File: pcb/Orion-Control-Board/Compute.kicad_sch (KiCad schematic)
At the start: 20 parts, among them J10 POWER, J2 NUCLEO64_CN7, J3 JETSON_ORIN_NANO_DEVKIT_GPIO, J4 5V Select Socket, J5 5V Select Jumper, J6 NUCLEO64_CN10, J7 I2C 1, J8 I2C 3, J9 UART

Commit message: Update symbols
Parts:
- J10, J5, J7, J8, J9: footprint AA_Custom_Components:Jumper_PinHeader_1x03_P2.54mm_Vertical -> digikey-footprints:PinHeader_1x3_P2.54_Drill1.1mm
- J4: footprint Connector_PinSocket_2.54mm:PinSocket_1x03_P2.54mm_Vertical -> digikey-footprints:PinHeader_1x3_P2.54_Drill1.1mm
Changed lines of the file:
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@@
 	)
 	(symbol
-		(lib_name "MountingHole_4")
 		(lib_id "Mechanical:MountingHole")
 		(at 162.56 25.4 0)
@@
 			)
 		)
-		(property "Description" ""
+		(property "Description" "Mounting Hole without connection"
 			(at 162.56 25.4 0)
 			(effects
@@
 					(size 1.27 1.27)
 				)
+				(hide yes)
 			)
 		)
@@
 	)
 	(symbol
-		(lib_name "MountingHole_3")
 		(lib_id "Mechanical:MountingHole")
 		(at 182.88 25.4 0)
@@
 			)
 		)
-		(property "Description" ""
+		(property "Description" "Mounting Hole without connection"
 			(at 182.88 25.4 0)
 			(effects
@@
 					(size 1.27 1.27)
 				)
+				(hide yes)
 			)
 		)
@@
 	)
 	(symbol
-		(lib_name "MountingHole_2")
 		(lib_id "Mechanical:MountingHole")
 		(at 162.56 31.75 0)
@@
 			)
 		)
-		(property "Description" ""
+		(property "Description" "Mounting Hole without connection"
 			(at 162.56 31.75 0)
 			(effects
@@
 					(size 1.27 1.27)
 				)
+				(hide yes)
 			)
 		)
@@
 	)
 	(symbol
-		(lib_name "MountingHole_1")
 		(lib_id "Mechanical:MountingHole")
 		(at 182.88 31.75 0)
@@
 			)
 		)
-		(property "Description" ""
+		(property "Description" "Mounting Hole without connection"
 			(at 182.88 31.75 0)
 			(effects
@@
 					(size 1.27 1.27)
 				)
+				(hide yes)
 			)
 		)
@@
 	)
 	(symbol
-		(lib_name "MountingHole_2")
 		(lib_id "Mechanical:MountingHole")
 		(at 229.87 25.4 0)
@@
 			)
 		)
-		(property "Description" ""
+		(property "Description" "Mounting Hole without connection"
 			(at 229.87 25.4 0)
 			(effects
@@
 			)
 		)
-		(property "Description" ""
+		(property "Description" "Power symbol creates a global label with name \"+5VD\""
 			(at 125.73 72.39 0)
 			(effects
@@
 					(size 1.27 1.27)
 				)
+				(hide yes)
 			)
 		)
@@
 			)
 		)
-		(property "Footprint" "AA_Custom_Components:Jumper_PinHeader_1x03_P2.54mm_Vertical"
+		(property "Footprint" "digikey-footprints:PinHeader_1x3_P2.54_Drill1.1mm"
 			(at 152.4 72.39 0)
 			(effects
@@
 			)
 		)
-		(property "Description" ""
+		(property "Description" "Ground Supply (Earth Ground style) Ground supply with a traditional \"earth ground\" symbol."
 			(at 172.72 72.39 0)
 			(effects
@@
 					(size 1.27 1.27)
 				)
+				(hide yes)
 			)
 		)
@@
 			)
 		)
-		(property "Description" ""
+		(property "Description" "Power symbol creates a global label with name \"+3.3V\""
 			(at 185.42 87.63 0)
 			(effects
@@
 					(size 1.27 1.27)
 				)
+				(hide yes)
 			)
 		)
@@
 	)
 	(symbol
-		(lib_name "MountingHole_3")
 		(lib_id "Mechanical:MountingHole")
 		(at 208.28 25.4 0)
@@
 			)
 		)
-		(property "Description" ""
+		(property "Description" "Mounting Hole without connection"
 			(at 208.28 25.4 0)
 			(effects
@@
 			)
 		)
-		(property "Description" ""
+		(property "Description" "Power symbol creates a global label with name \"+5VD\""
 			(at 64.77 68.58 0)
 			(effects
@@
 					(size 1.27 1.27)
 				)
+				(hide yes)
 			)
 		)
@@
 			)
 		)
-		(property "Description" ""
+		(property "Description" "Ground Supply (Earth Ground style) Ground supply with a traditional \"earth ground\" symbol."
 			(at 149.86 90.17 0)
 			(effects
@@
 					(size 1.27 1.27)
 				)
+				(hide yes)
 			)
 		)
@@
 			)
 		)
-		(property "Description" ""
+		(property "Description" "Ground Supply (Earth Ground style) Ground supply with a traditional \"earth ground\" symbol."
 			(at 149.86 72.39 0)
 			(effects
@@
 					(size 1.27 1.27)
 				)
+				(hide yes)
 			)
 		)
@@
 			)
 		)
-		(property "Description" ""
+		(property "Description" "Ground Supply (Earth Ground style) Ground supply with a traditional \"earth ground\" symbol."
 			(at 125.73 87.63 0)
 			(effects
@@
 					(size 1.27 1.27)
 				)
+				(hide yes)
 			)
 		)
@@
 			)
 		)
-		(property "Description" ""
+		(property "Description" "test point"
 			(at 128.27 22.86 0)
 			(effects
@@
 			)
 		)
-		(property "Description" ""
+		(property "Description" "Power symbol creates a global label with name \"+3.3V\""
 			(at 60.96 81.28 0)
 			(effects
@@
 					(size 1.27 1.27)
 				)
+				(hide yes)
 			)
 		)
@@
 			)
 		)
-		(property "Description" ""
+		(property "Description" "Power symbol creates a global label with name \"+5VD\""
 			(at 111.76 22.86 0)
 			(effects
@@
 					(size 1.27 1.27)
 				)
+				(hide yes)
 			)
 		)
@@
 			)
 		)
-		(property "Description" ""
+		(property "Description" "test point"
 			(at 111.76 22.86 0)
 			(effects
@@
 			)
 		)
-		(property "Description" ""
+		(property "Description" "test point"
 			(at 144.78 20.32 0)
 			(effects
@@
 			)
 		)
-		(property "Footprint" "Connector_PinSocket_2.54mm:PinSocket_1x03_P2.54mm_Vertical"
+		(property "Footprint" "digikey-footprints:PinHeader_1x3_P2.54_Drill1.1mm"
 			(at 102.87 34.29 0)
 			(effects
@@
 			)
 		)
-		(property "Description" ""
+		(property "Description" "Power symbol creates a global label with name \"+5VD\""
 			(at 179.07 85.09 0)
 			(effects
@@
 					(size 1.27 1.27)
 				)
+				(hide yes)
 			)
 		)
@@
 			)
 		)
-		(property "Footprint" "AA_Custom_Components:Jumper_PinHeader_1x03_P2.54mm_Vertical"
+		(property "Footprint" "digikey-footprints:PinHeader_1x3_P2.54_Drill1.1mm"
 			(at 175.26 90.17 0)
 			(effects
@@
 			)
 		)
-		(property "Description" ""
+		(property "Description" "Power symbol creates a global label with name \"+3.3V\""
 			(at 128.27 22.86 0)
 			(effects
@@
 					(size 1.27 1.27)
 				)
+				(hide yes)
 			)
 		)
@@
 			)
 		)
-		(property "Footprint" "AA_Custom_Components:Jumper_PinHeader_1x03_P2.54mm_Vertical"
+		(property "Footprint" "digikey-footprints:PinHeader_1x3_P2.54_Drill1.1mm"
 			(at 152.4 90.17 0)
 			(effects
@@
 			)
 		)
-		(property "Description" ""
+		(property "Description" "Ground Supply (Earth Ground style) Ground supply with a traditional \"earth ground\" symbol."
 			(at 17.78 86.36 0)
 			(effects
@@
 					(size 1.27 1.27)
 				)
+				(hide yes)
 			)
 		)
@@
 			)
 		)
-		(property "Description" ""
+		(property "Description" "Ground Supply (Earth Ground style) Ground supply with a traditional \"earth ground\" symbol."
 			(at 62.23 104.14 0)
 			(effects
@@
 					(size 1.27 1.27)
 				)
+				(hide yes)
 			)
 		)
@@
 			)
 		)
-		(property "Footprint" "AA_Custom_Components:Jumper_PinHeader_1x03_P2.54mm_Vertical"
+		(property "Footprint" "digikey-footprints:PinHeader_1x3_P2.54_Drill1.1mm"
 			(at 175.26 72.39 0)
 			(effects
@@
 			)
 		)
-		(property "Description" ""
+		(property "Description" "Ground Supply (Earth Ground style) Ground supply with a traditional \"earth ground\" symbol."
 			(at 72.39 90.17 0)
 			(effects
@@
 					(size 1.27 1.27)
 				)
+				(hide yes)
 			)
 		)
@@
 			)
 		)
-		(property "Footprint" "AA_Custom_Components:Jumper_PinHeader_1x03_P2.54mm_Vertical"
+		(property "Footprint" "digikey-footprints:PinHeader_1x3_P2.54_Drill1.1mm"
 			(at 113.03 34.29 0)
 			(effects
@@
 			)
 		)
-		(property "Description" ""
+		(property "Description" "Ground Supply (Earth Ground style) Ground supply with a traditional \"earth ground\" symbol."
 			(at 172.72 90.17 0)
 			(effects
@@
 					(size 1.27 1.27)
 				)
+				(hide yes)
 			)
 		)
@@
 			)
 		)
-		(property "Description" ""
+		(property "Description" "Buzzer, polarized"
 			(at 64.77 99.06 0)
 			(effects
@@
 					(size 1.27 1.27)
 				)
+				(hide yes)
 			)
 		)
@@
 			)
 		)
-		(property "Description" ""
+		(property "Description" "Ground Supply (Earth Ground style) Ground supply with a traditional \"earth ground\" symbol."
 			(at 31.75 38.1 0)
 			(effects
@@
 					(size 1.27 1.27)
 				)
+				(hide yes)
 			)
 		)
@@
 	)
 	(symbol
-		(lib_name "MountingHole_1")
 		(lib_id "Mechanical:MountingHole")
 		(at 208.28 31.75 0)
@@
 			)
 		)
-		(property "Description" ""
+		(property "Description" "Mounting Hole without connection"
 			(at 208.28 31.75 0)
 			(effects

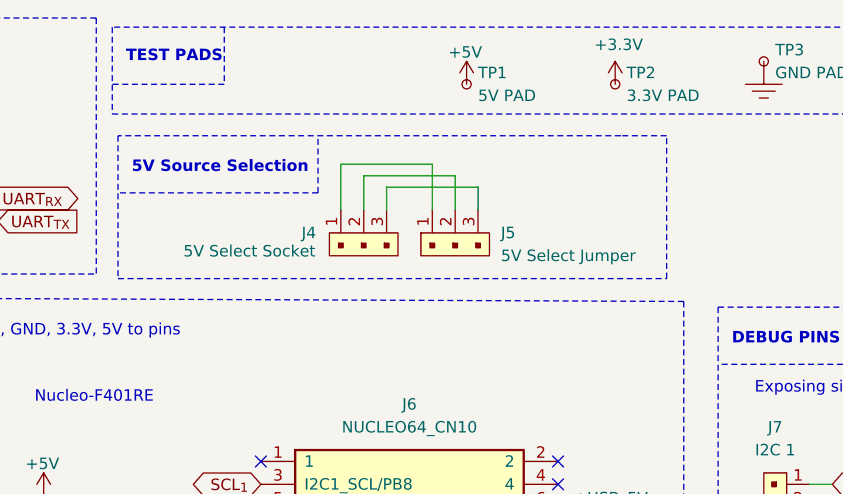
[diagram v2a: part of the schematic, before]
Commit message: Route IMU and Servo Driver
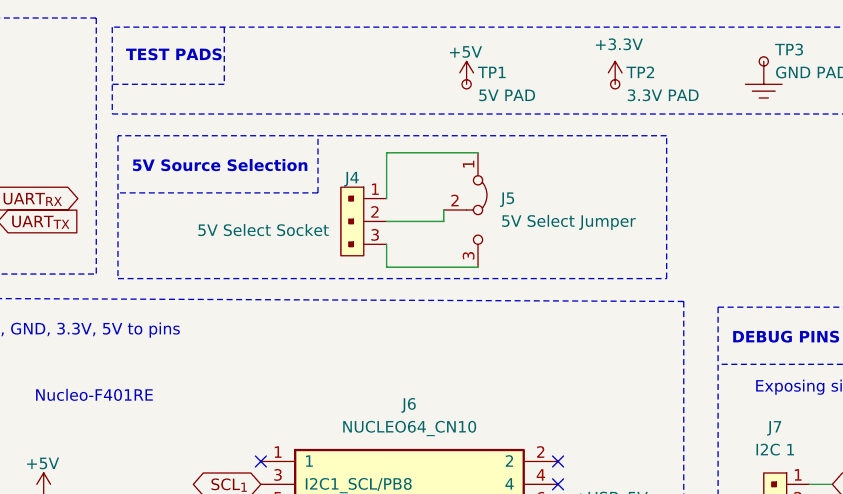
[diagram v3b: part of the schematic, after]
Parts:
- removed J5: 5V Select Jumper, digikey-footprints:PinHeader_1x3_P2.54_Drill1.1mm, symbol dk_Rectangular-Connectors-Headers-Male-Pins:640456-3
- added J5: 5V Select Jumper, AA_Custom_Components:Jumper_PinHeader_1x03_P2.54mm_Vertical_Bridged, symbol Jumper:Jumper_3_Bridged12
- J4: footprint digikey-footprints:PinHeader_1x3_P2.54_Drill1.1mm -> Connector_PinSocket_2.54mm:PinSocket_1x03_P2.54mm_Vertical
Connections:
- net at J4.1: now also J5.1 (A)
- net at J4.2: now also J5.2 (C)
- net at J4.3: now also J5.3 (B)
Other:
- moved on the sheet: J4

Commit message: Route more
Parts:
- J9: footprint digikey-footprints:PinHeader_1x3_P2.54_Drill1.1mm -> Connector_PinHeader_2.54mm:PinHeader_1x03_P2.54mm_Vertical
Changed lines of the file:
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@@
 			)
 		)
-		(property "Footprint" "digikey-footprints:PinHeader_1x3_P2.54_Drill1.1mm"
+		(property "Footprint" "Connector_PinHeader_2.54mm:PinHeader_1x03_P2.54mm_Vertical"
 			(at 175.26 72.39 0)
 			(effects

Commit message: Route most traces
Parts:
- removed H1, H2, H3, H4: MountingHole, MountingHole:MountingHole_3.2mm_M3_Pad, symbol Mechanical:MountingHole
- added N1: ORION_LOGO, Orion-Logo:Orion-Logo-20mm, symbol Mechanical:Housing
- J10, J7, J8: footprint digikey-footprints:PinHeader_1x3_P2.54_Drill1.1mm -> Connector_PinHeader_2.54mm:PinHeader_1x03_P2.54mm_Vertical
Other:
- note added: "PCB LOGO"
- note removed: "MOUNTING"
- moved on the sheet: H5, H6, H7, J10, J7, J8, J9

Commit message: Finalize Fab outputs
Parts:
- BZ1, H5, H6, H7, J10, J2, J3, J4, J6, J7, J8, J9, N1, TP1, TP2, TP3: now not fitted
- J5: now not fitted; now in the parts list

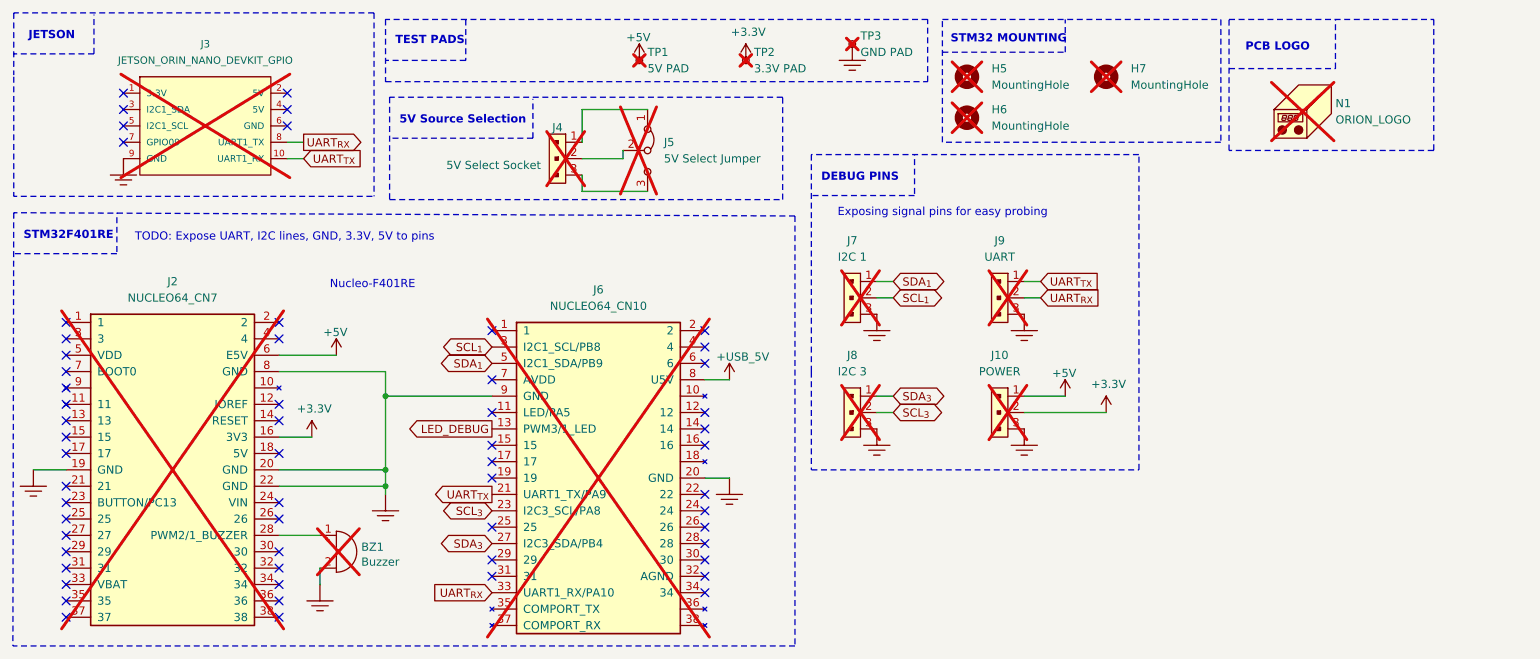
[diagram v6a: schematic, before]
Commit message: Add screen step model
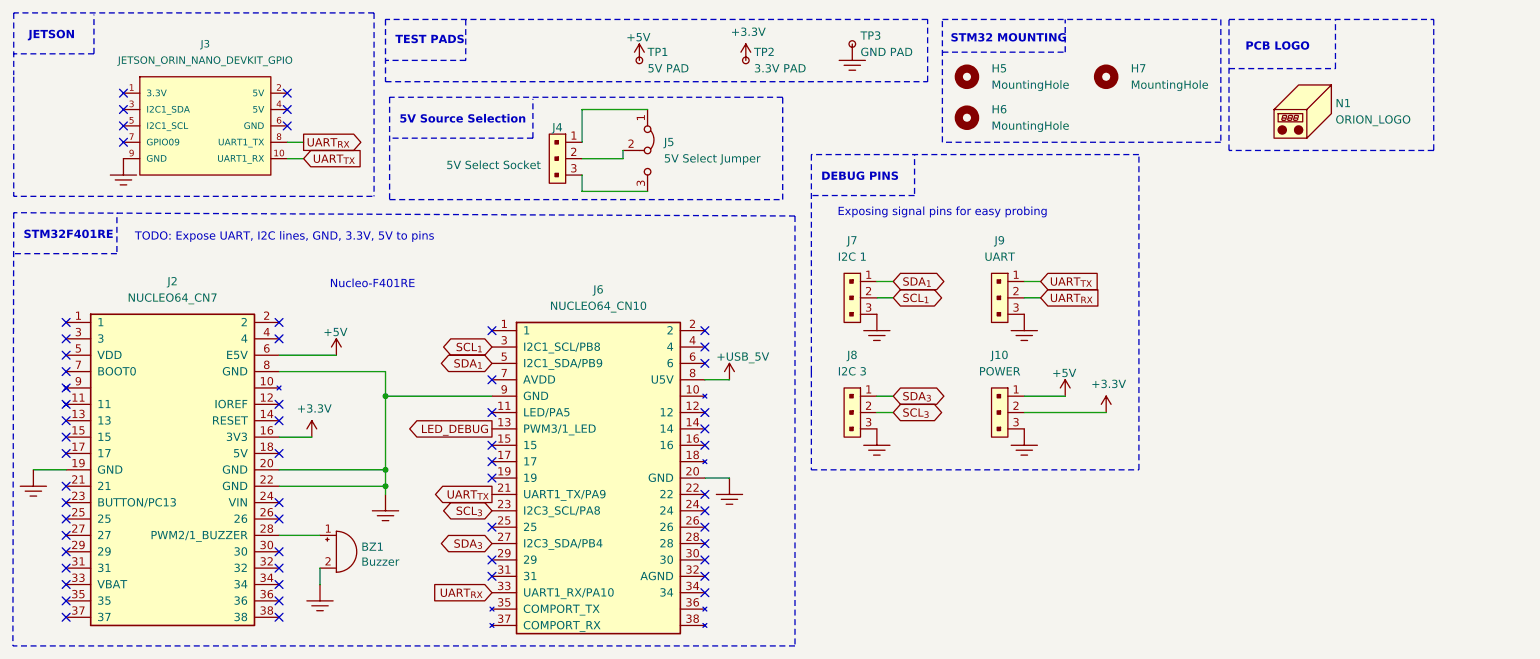
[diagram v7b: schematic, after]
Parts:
- BZ1, H5, H6, H7, J10, J2, J3, J4, J5, J6, J7, J8, J9, N1, TP1, TP2, TP3: now fitted
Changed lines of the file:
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@@
 		(in_bom yes)
 		(on_board yes)
-		(dnp yes)
+		(dnp no)
 		(fields_autoplaced yes)
 		(property "Reference" "H7"
@@
 		(in_bom yes)
 		(on_board yes)
-		(dnp yes)
+		(dnp no)
 		(fields_autoplaced yes)
 		(property "Reference" "J7"
@@
 		(in_bom yes)
 		(on_board yes)
-		(dnp yes)
+		(dnp no)
 		(fields_autoplaced yes)
 		(property "Reference" "H5"
@@
 		(in_bom yes)
 		(on_board yes)
-		(dnp yes)
+		(dnp no)
 		(fields_autoplaced yes)
 		(property "Reference" "J5"
@@
 		(in_bom yes)
 		(on_board yes)
-		(dnp yes)
+		(dnp no)
 		(fields_autoplaced yes)
 		(property "Reference" "N1"
@@
 		(in_bom yes)
 		(on_board yes)
-		(dnp yes)
+		(dnp no)
 		(fields_autoplaced yes)
 		(property "Reference" "TP2"
@@
 		(in_bom yes)
 		(on_board yes)
-		(dnp yes)
+		(dnp no)
 		(fields_autoplaced yes)
 		(property "Reference" "TP1"
@@
 		(in_bom yes)
 		(on_board yes)
-		(dnp yes)
+		(dnp no)
 		(fields_autoplaced yes)
 		(property "Reference" "TP3"
@@
 		(in_bom yes)
 		(on_board yes)
-		(dnp yes)
+		(dnp no)
 		(property "Reference" "J4"
 			(at 99.06 33.274 90)
@@
 		(in_bom yes)
 		(on_board yes)
-		(dnp yes)
+		(dnp no)
 		(fields_autoplaced yes)
 		(property "Reference" "J2"
@@
 		(in_bom yes)
 		(on_board yes)
-		(dnp yes)
+		(dnp no)
 		(fields_autoplaced yes)
 		(property "Reference" "J10"
@@
 		(in_bom yes)
 		(on_board yes)
-		(dnp yes)
+		(dnp no)
 		(fields_autoplaced yes)
 		(property "Reference" "J8"
@@
 		(in_bom yes)
 		(on_board yes)
-		(dnp yes)
+		(dnp no)
 		(fields_autoplaced yes)
 		(property "Reference" "J9"
@@
 		(in_bom yes)
 		(on_board yes)
-		(dnp yes)
+		(dnp no)
 		(fields_autoplaced yes)
 		(property "Reference" "J6"
@@
 		(in_bom yes)
 		(on_board yes)
-		(dnp yes)
+		(dnp no)
 		(property "Reference" "BZ1"
 			(at 68.6308 98.3234 0)
@@
 		(in_bom yes)
 		(on_board yes)
-		(dnp yes)
+		(dnp no)
 		(fields_autoplaced yes)
 		(property "Reference" "J3"
@@
 		(in_bom yes)
 		(on_board yes)
-		(dnp yes)
+		(dnp no)
 		(fields_autoplaced yes)
 		(property "Reference" "H6"
